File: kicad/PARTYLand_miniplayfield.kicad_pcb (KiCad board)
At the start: 2 copper layers, 18 parts, among them P1 CONN_6, U1 74HC595

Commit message: Creating silk footprints with the party land artwork in order to place the LEDs correctly in the PCB. The holes/layout footprint is intended to be used as the board outline so the PCB will hav ethis special playfield shape.
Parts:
- added G***: LOGO, partyland:playfield_inserts, F.Cu at (129.5, 76.2)
- moved R6 131.4 mm to (33.0, 167.6), turned to 90 degrees
- moved P1 131.2 mm to (15.2, 189.2)
- moved R3 122.7 mm to (38.1, 167.6), turned to 90 degrees
- moved R8 122.5 mm to (43.2, 167.6), turned to 90 degrees
- moved R4 120.0 mm to (53.3, 167.6), turned to 90 degrees
- moved U1 114.9 mm to (50.8, 185.4), turned to 180 degrees
- moved R2 109.8 mm to (58.4, 167.6), turned to 90 degrees
- moved R1 107.2 mm to (48.3, 167.6), turned to 90 degrees
- moved R5 105.6 mm to (63.5, 167.6), turned to 90 degrees
- moved R7 101.5 mm to (68.6, 167.6), turned to 90 degrees
- moved D6 85.7 mm to (65.5, 126.5)
- moved D7 65.7 mm to (125.2, 166.5)
- moved D8 52.6 mm to (186.1, 126.1)
- moved D2 46.6 mm to (114.8, 137.1)
- moved D3 45.5 mm to (125.6, 134.6)
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
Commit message: Added the playfield outline (footprint drawing, still not the actual drill outline) Also tweaked the PCB metadata and the overall footprints positioning.
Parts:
- added G***: LOGO, partyland:playfield_holes, F.Cu at (125.0, 204.2)
- moved R1 156.6 mm to (91.2, 318.2)
- moved R2 156.6 mm to (101.3, 318.2)
- moved R3 156.6 mm to (81.0, 318.2)
- moved R4 156.6 mm to (96.3, 318.2)
- moved R5 156.6 mm to (106.4, 318.2)
- moved R6 156.6 mm to (76.0, 318.2)
- moved R7 156.6 mm to (111.5, 318.2)
- moved R8 156.6 mm to (86.1, 318.2)
- moved P1 153.9 mm to (65.8, 334.6)
- moved U1 153.8 mm to (88.8, 334.5)
- moved D1 129.6 mm to (98.8, 264.2)
- moved D8 129.6 mm to (180.8, 255.6)
- moved G*** 129.6 mm to (124.2, 205.7)
- moved D2 129.6 mm to (109.5, 266.7)
- moved D3 129.6 mm to (120.3, 264.1)
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
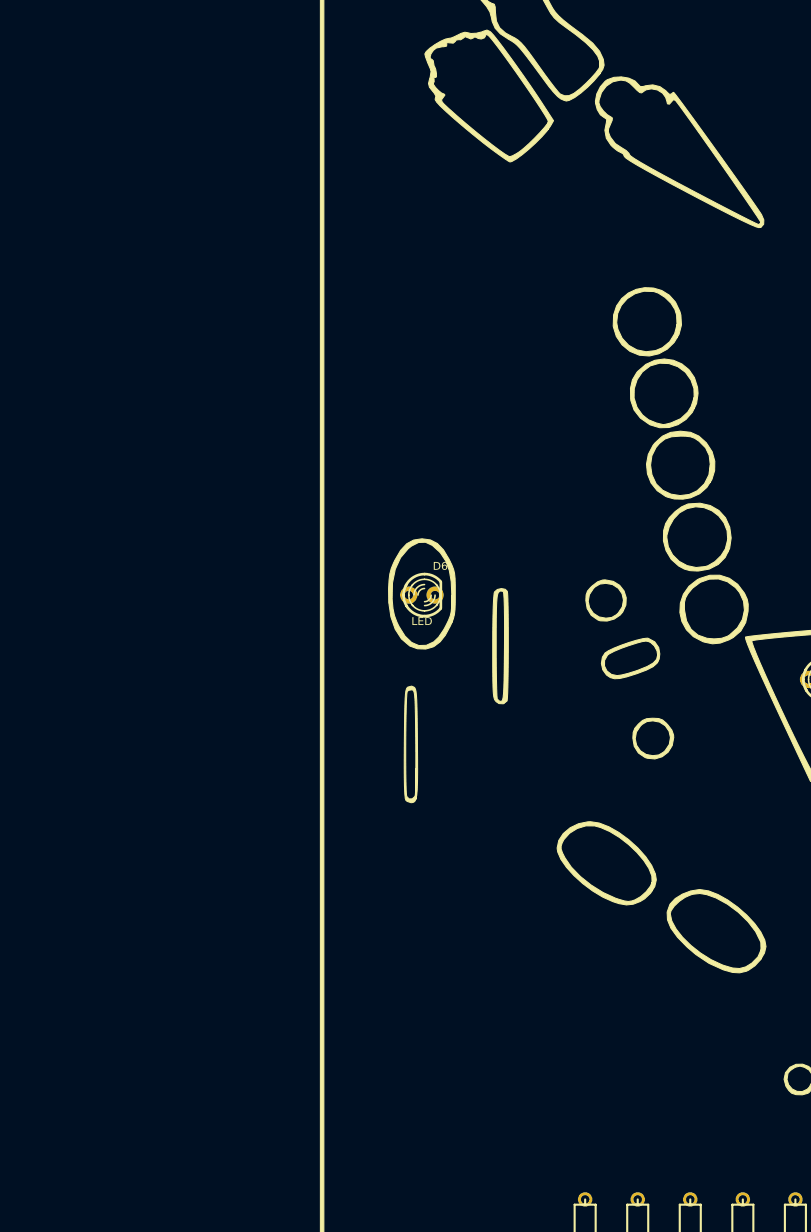
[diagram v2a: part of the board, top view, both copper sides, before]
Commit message: Added a second group of LEDs using a second daisychained shift register. WIP on positioning the footprints on the PCB
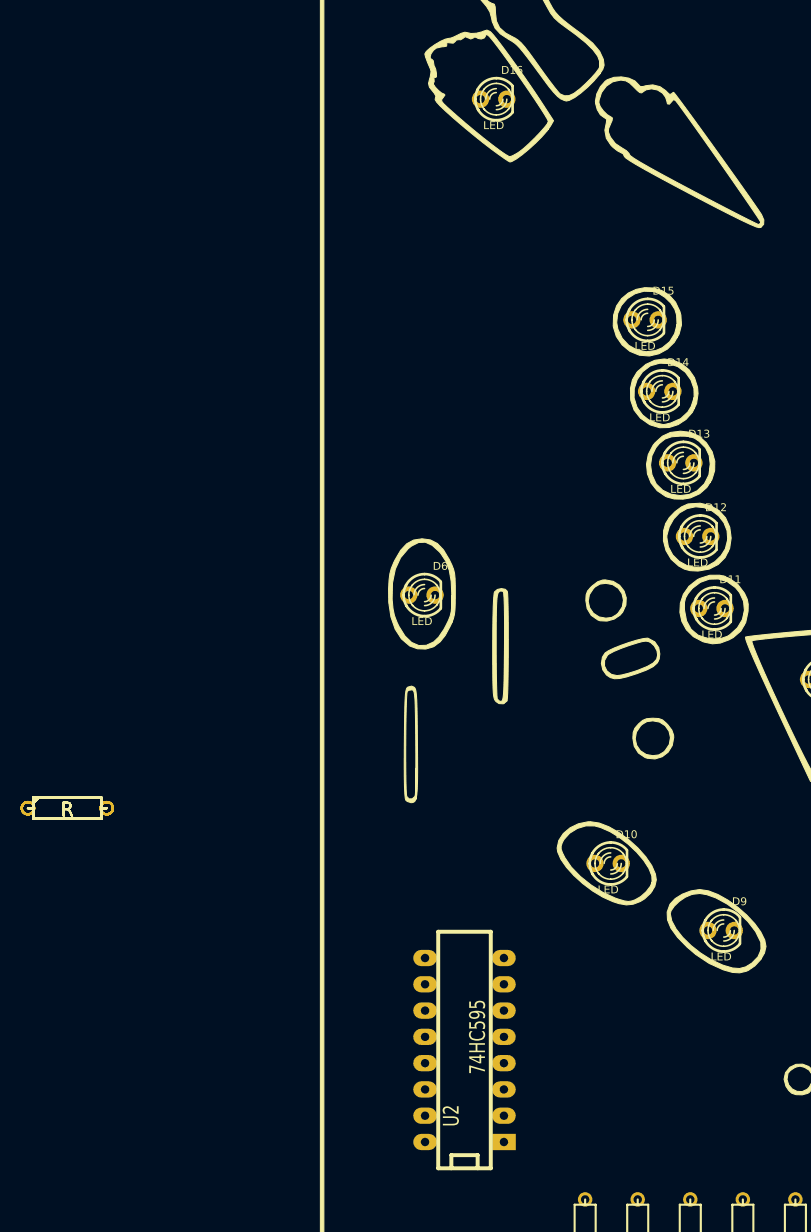
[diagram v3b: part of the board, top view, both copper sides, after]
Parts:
- added D10: LED, LEDs:LED-3MM, F.Cu at (78.2, 281.9)
- added D11: LED, LEDs:LED-3MM, F.Cu at (88.2, 257.3)
- added D12: LED, LEDs:LED-3MM, F.Cu at (86.8, 250.3)
- added D13: LED, LEDs:LED-3MM, F.Cu at (85.2, 243.2)
- added D14: LED, LEDs:LED-3MM, F.Cu at (83.2, 236.3)
- added D15: LED, LEDs:LED-3MM, F.Cu at (81.7, 229.4)
- added D16: LED, LEDs:LED-3MM, F.Cu at (67.1, 208.1)
- added D9: LED, LEDs:LED-3MM, F.Cu at (89.1, 288.4)
- added R10, R11, R12, R13, R14, R15, R16, R9: R, Discret:R3, F.Cu at (25.9, 276.6)
- added U2: 74HC595, Sockets_DIP:DIP-16__300_ELL, F.Cu at (64.3, 300.0)
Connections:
- U1 pad 9: Net-(U1-Pad9) -> LED_SERIAL_DATA_CHAIN2

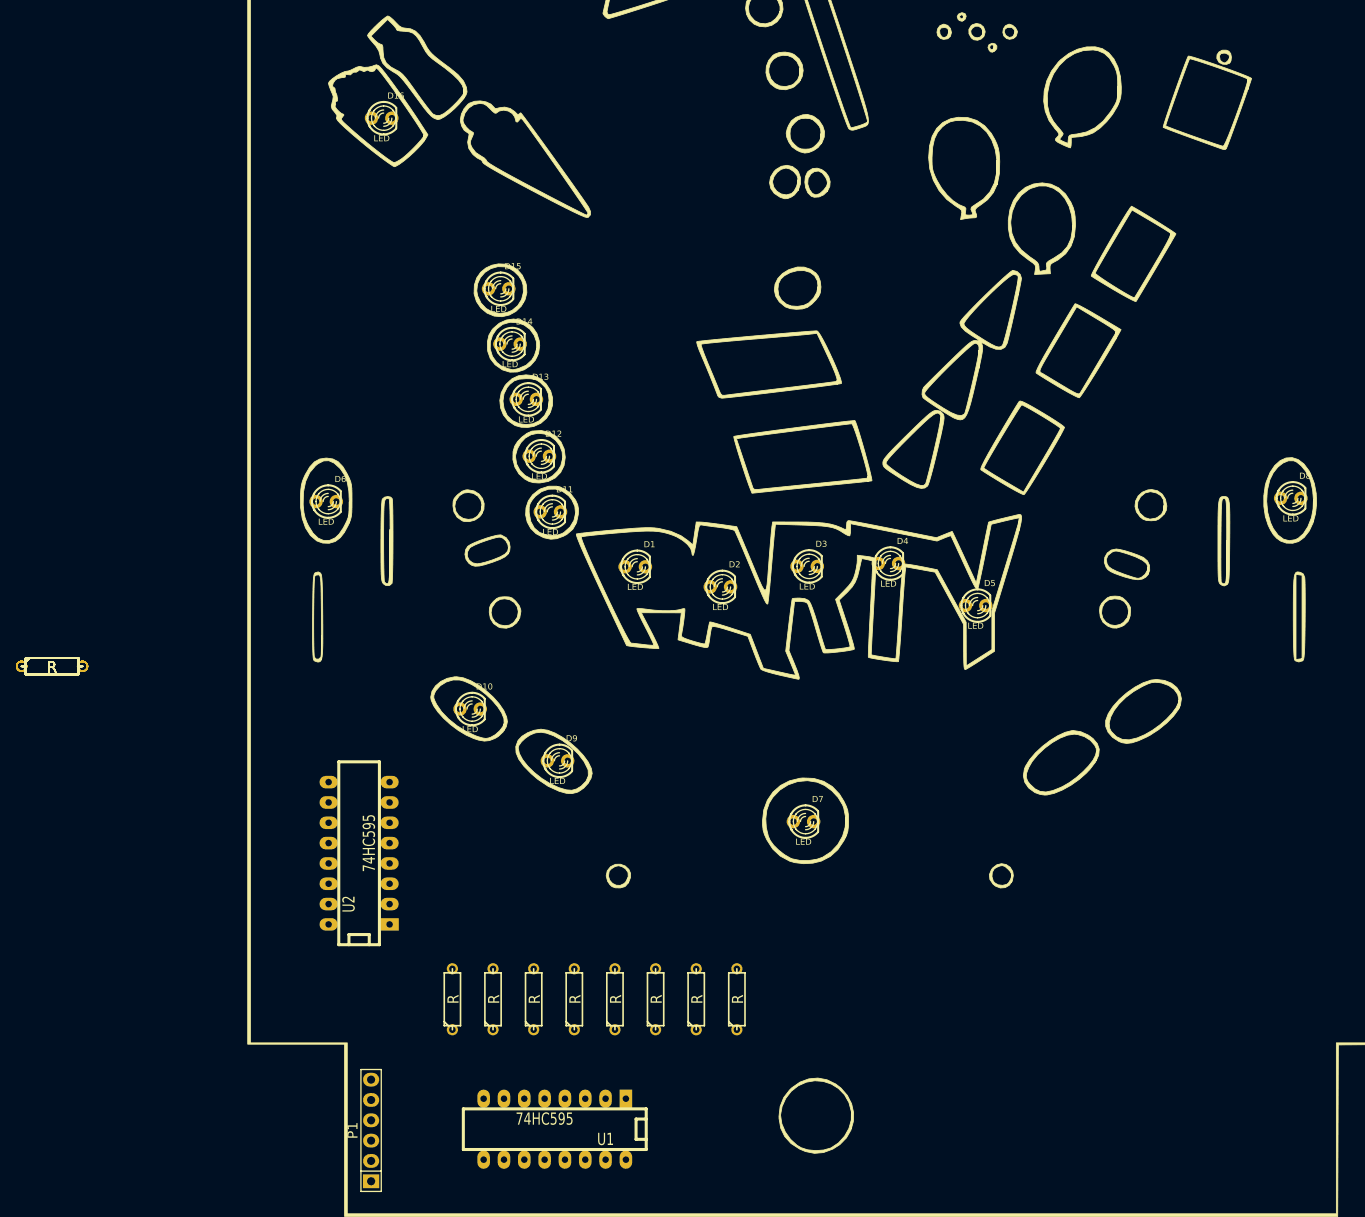
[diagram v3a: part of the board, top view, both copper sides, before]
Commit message: Adding more LED circuitry to the PARTYLand miniplayfield.
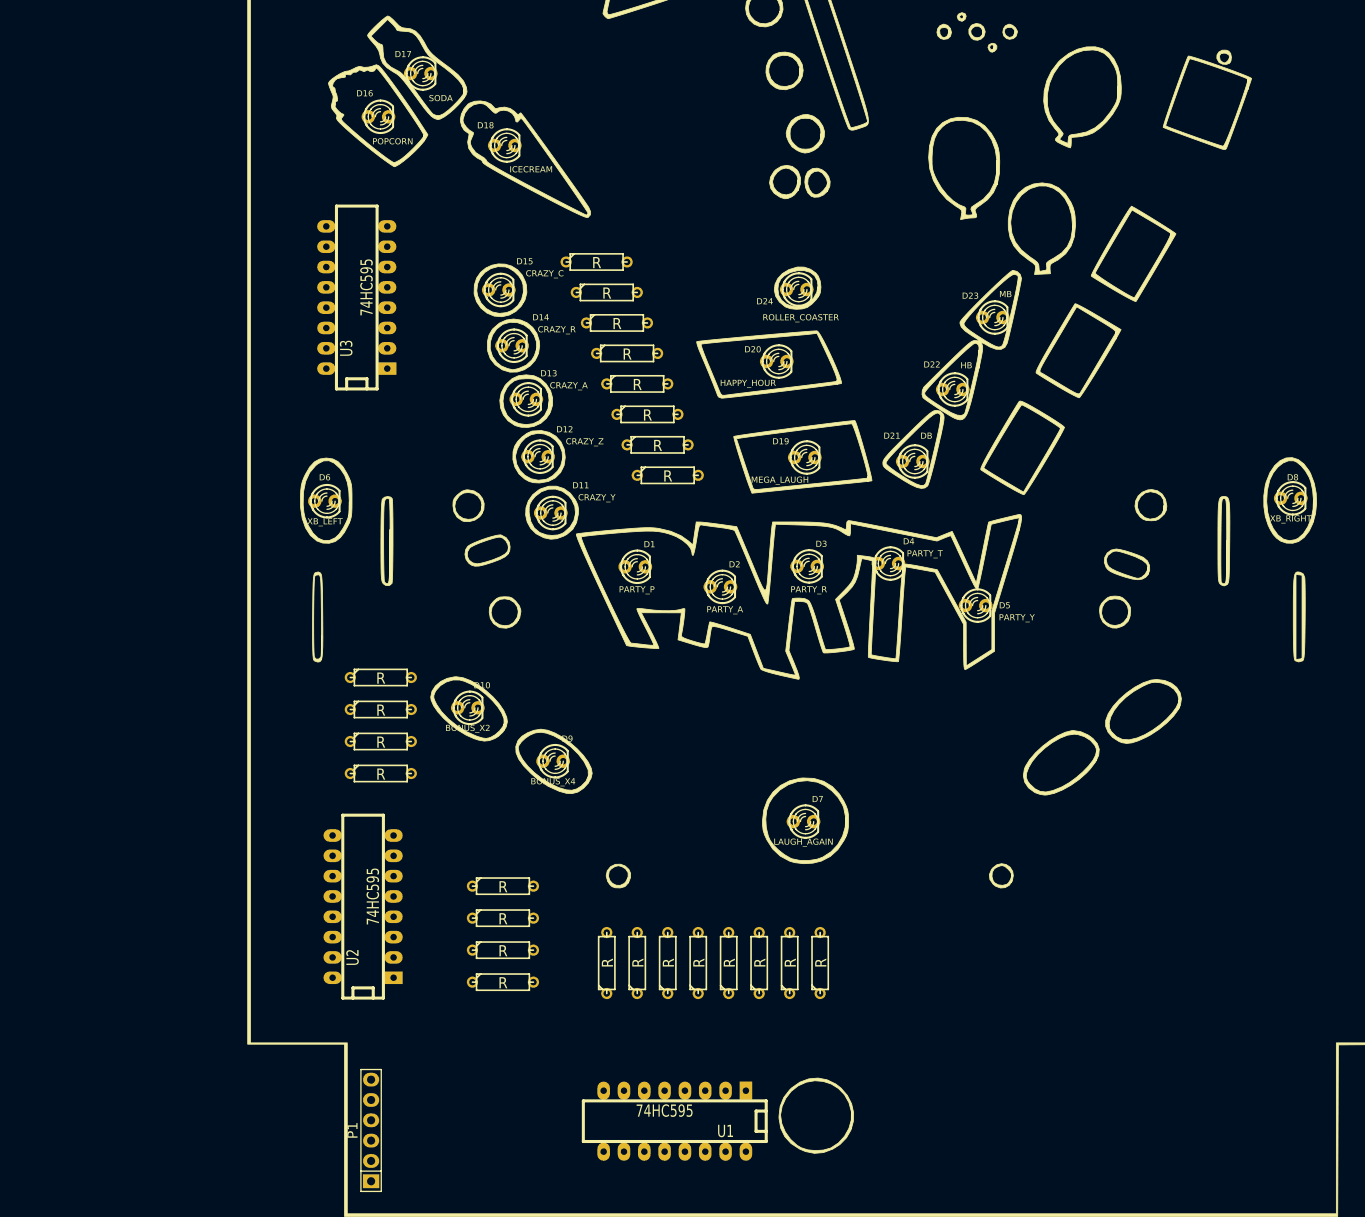
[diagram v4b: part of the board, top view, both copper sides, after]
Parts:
- added D17: SODA, LEDs:LED-3MM, F.Cu at (72.0, 202.5)
- added D18: ICECREAM, LEDs:LED-3MM, F.Cu at (82.5, 211.5)
- added D19: MEGA_LAUGH, LEDs:LED-3MM, F.Cu at (120.0, 250.5)
- added D20: HAPPY_HOUR, LEDs:LED-3MM, F.Cu at (116.5, 238.5)
- added D21: DB, LEDs:LED-3MM, F.Cu at (133.5, 251.0)
- added D22: HB, LEDs:LED-3MM, F.Cu at (138.5, 242.0)
- added D23: MB, LEDs:LED-3MM, F.Cu at (143.5, 233.0)
- added D24: ROLLER_COASTER, LEDs:LED-3MM, F.Cu at (119.0, 229.5)
- added R17: R, Discret:R3, F.Cu at (102.9, 252.7)
- added R18: R, Discret:R3, F.Cu at (101.6, 248.9)
- added R19: R, Discret:R3, F.Cu at (100.3, 245.1)
- added R20: R, Discret:R3, F.Cu at (99.1, 241.3)
- added R21: R, Discret:R3, F.Cu at (97.8, 237.5)
- added R22: R, Discret:R3, F.Cu at (96.5, 233.7)
- added R23: R, Discret:R3, F.Cu at (95.2, 229.9)
- added R24: R, Discret:R3, F.Cu at (94.0, 226.1)
- added U3: 74HC595, Sockets_DIP:DIP-16__300_ELL, F.Cu at (64.0, 230.5)
- D1: value LED -> PARTY_P
- D10: value LED -> BONUS_X2
- D11: value LED -> CRAZY_Y
- D12: value LED -> CRAZY_Z
- D13: value LED -> CRAZY_A
- D14: value LED -> CRAZY_R
- D15: value LED -> CRAZY_C
- D16: value LED -> POPCORN
- D2: value LED -> PARTY_A
- D3: value LED -> PARTY_R
- D4: value LED -> PARTY_T
- D5: value LED -> PARTY_Y
- D6: value LED -> XB_LEFT
- D7: value LED -> LAUGH_AGAIN
- D8: value LED -> XB_RIGHT
- D9: value LED -> BONUS_X4
- moved R9 68.8 mm to (82.3, 316.1)
- moved R10 66.6 mm to (82.3, 312.1)
- moved R11 64.6 mm to (82.3, 308.1)
- moved R12 62.7 mm to (82.3, 304.1)
- moved R13 43.2 mm to (67.0, 290.0)
- moved R14 42.2 mm to (67.0, 286.0)
- moved R15 41.4 mm to (67.0, 282.0)
- moved R16 41.1 mm to (67.0, 278.0)
- moved R3 33.6 mm to (114.3, 313.7)
- moved R1 31.1 mm to (121.9, 313.7)
- moved R6 27.3 mm to (102.9, 313.7)
- moved R2 17.4 mm to (118.1, 313.7)
- moved U1 15.0 mm to (103.8, 333.5)
- moved R4 14.9 mm to (110.5, 313.7)
- moved R7 13.2 mm to (99.1, 313.7)
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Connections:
- U2 pad 9: Net-(U2-Pad9) -> LED_SERIAL_DATA_CHAIN3

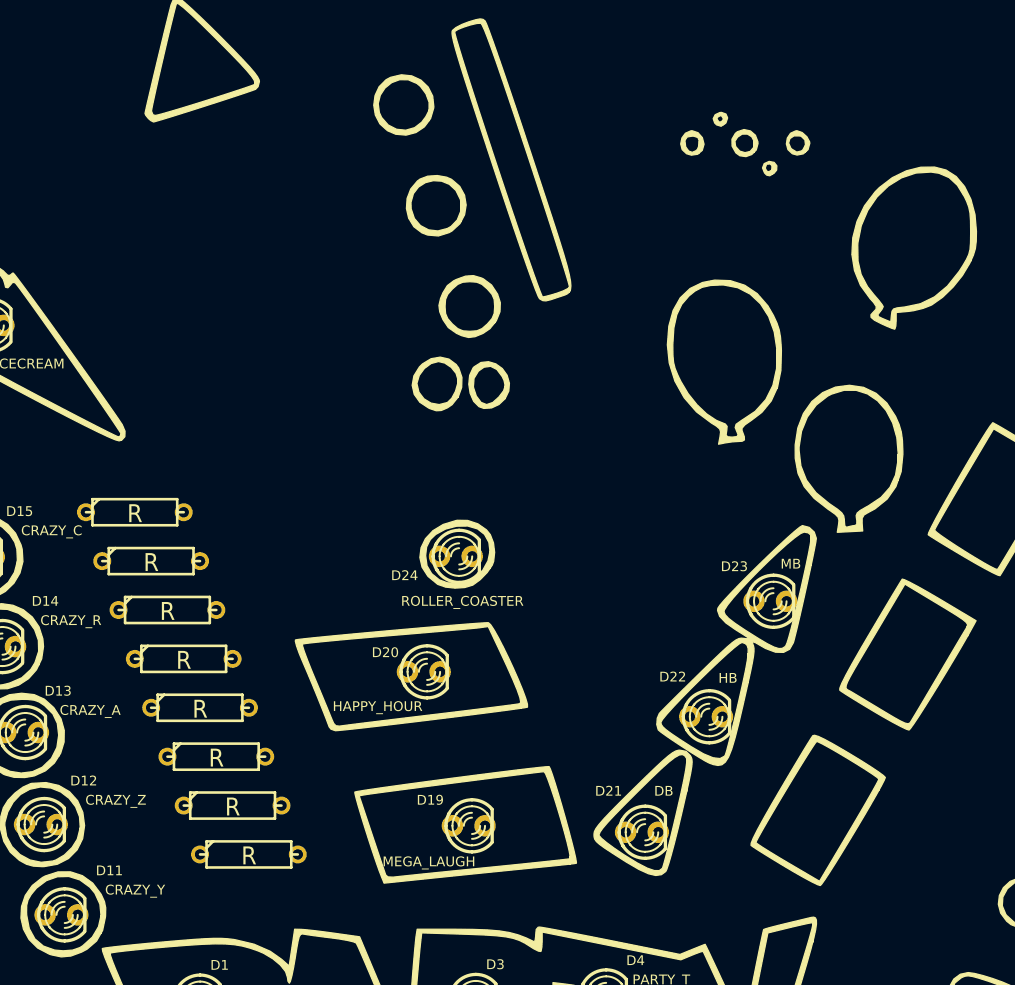
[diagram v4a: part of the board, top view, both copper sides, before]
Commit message: A few more LEDs in the PARTYLand mini-playfield PCB.
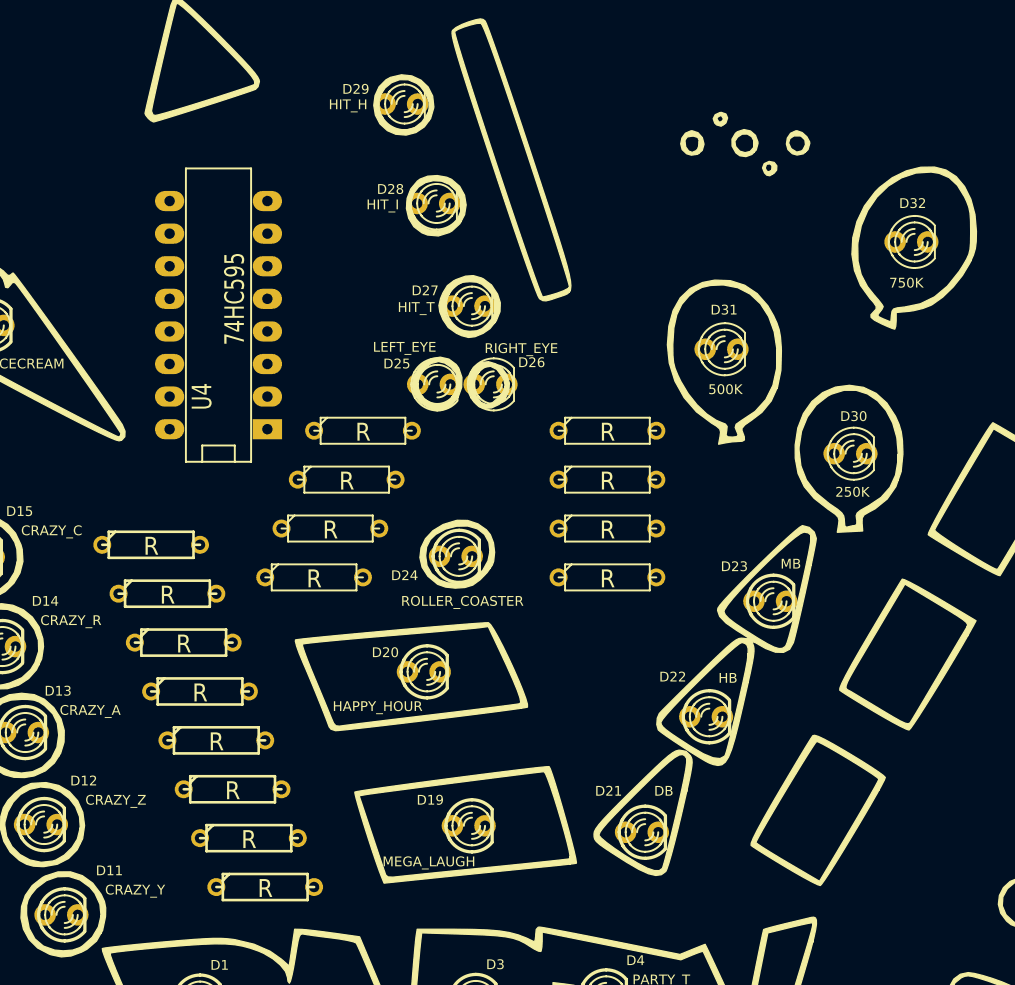
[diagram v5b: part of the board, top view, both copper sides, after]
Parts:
- added D25: LEFT_EYE, LEDs:LED-3MM, F.Cu at (117.3, 216.1)
- added D26: RIGHT_EYE, LEDs:LED-3MM, F.Cu at (121.7, 216.1)
- added D27: HIT_T, LEDs:LED-3MM, F.Cu at (120.0, 210.0)
- added D28: HIT_I, LEDs:LED-3MM, F.Cu at (117.2, 202.0)
- added D29: HIT_H, LEDs:LED-3MM, F.Cu at (114.8, 194.2)
- added D30: 250K, LEDs:LED-3MM, F.Cu at (149.8, 221.5)
- added D31: 500K, LEDs:LED-3MM, F.Cu at (139.7, 213.4)
- added D32: 750K, LEDs:LED-3MM, F.Cu at (154.5, 205.0)
- added R25: R, Discret:R3, F.Cu at (108.0, 231.1)
- added R26: R, Discret:R3, F.Cu at (109.2, 227.3)
- added R27: R, Discret:R3, F.Cu at (110.5, 223.5)
- added R28: R, Discret:R3, F.Cu at (111.8, 219.7)
- added R29: R, Discret:R3, F.Cu at (130.8, 231.1)
- added R30: R, Discret:R3, F.Cu at (130.8, 227.3)
- added R31: R, Discret:R3, F.Cu at (130.8, 223.5)
- added R32: R, Discret:R3, F.Cu at (130.8, 219.7)
- added U4: 74HC595, Sockets_DIP:DIP-16__300_ELL, F.Cu at (100.5, 210.7)
- moved R18 2.84 mm to (102.9, 251.5)
- moved R17 2.84 mm to (104.1, 255.3)
- moved R22 2.84 mm to (97.8, 236.2)
- moved R19 2.84 mm to (101.6, 247.7)
- moved R20 2.84 mm to (100.3, 243.8)
- moved R21 2.84 mm to (99.1, 240.0)
- moved R23 2.84 mm to (96.5, 232.4)
- moved R24 2.84 mm to (95.2, 228.6)
